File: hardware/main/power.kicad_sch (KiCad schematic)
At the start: 32 parts, among them Q1 SSM3J338R, Q2 BCP53, Q3 SSM3J338R, Q4 BC817, Q5 SSM3J338R, Q6 BC807, Q7 BC817, U5 AP2114H-3.3, U6 LM358

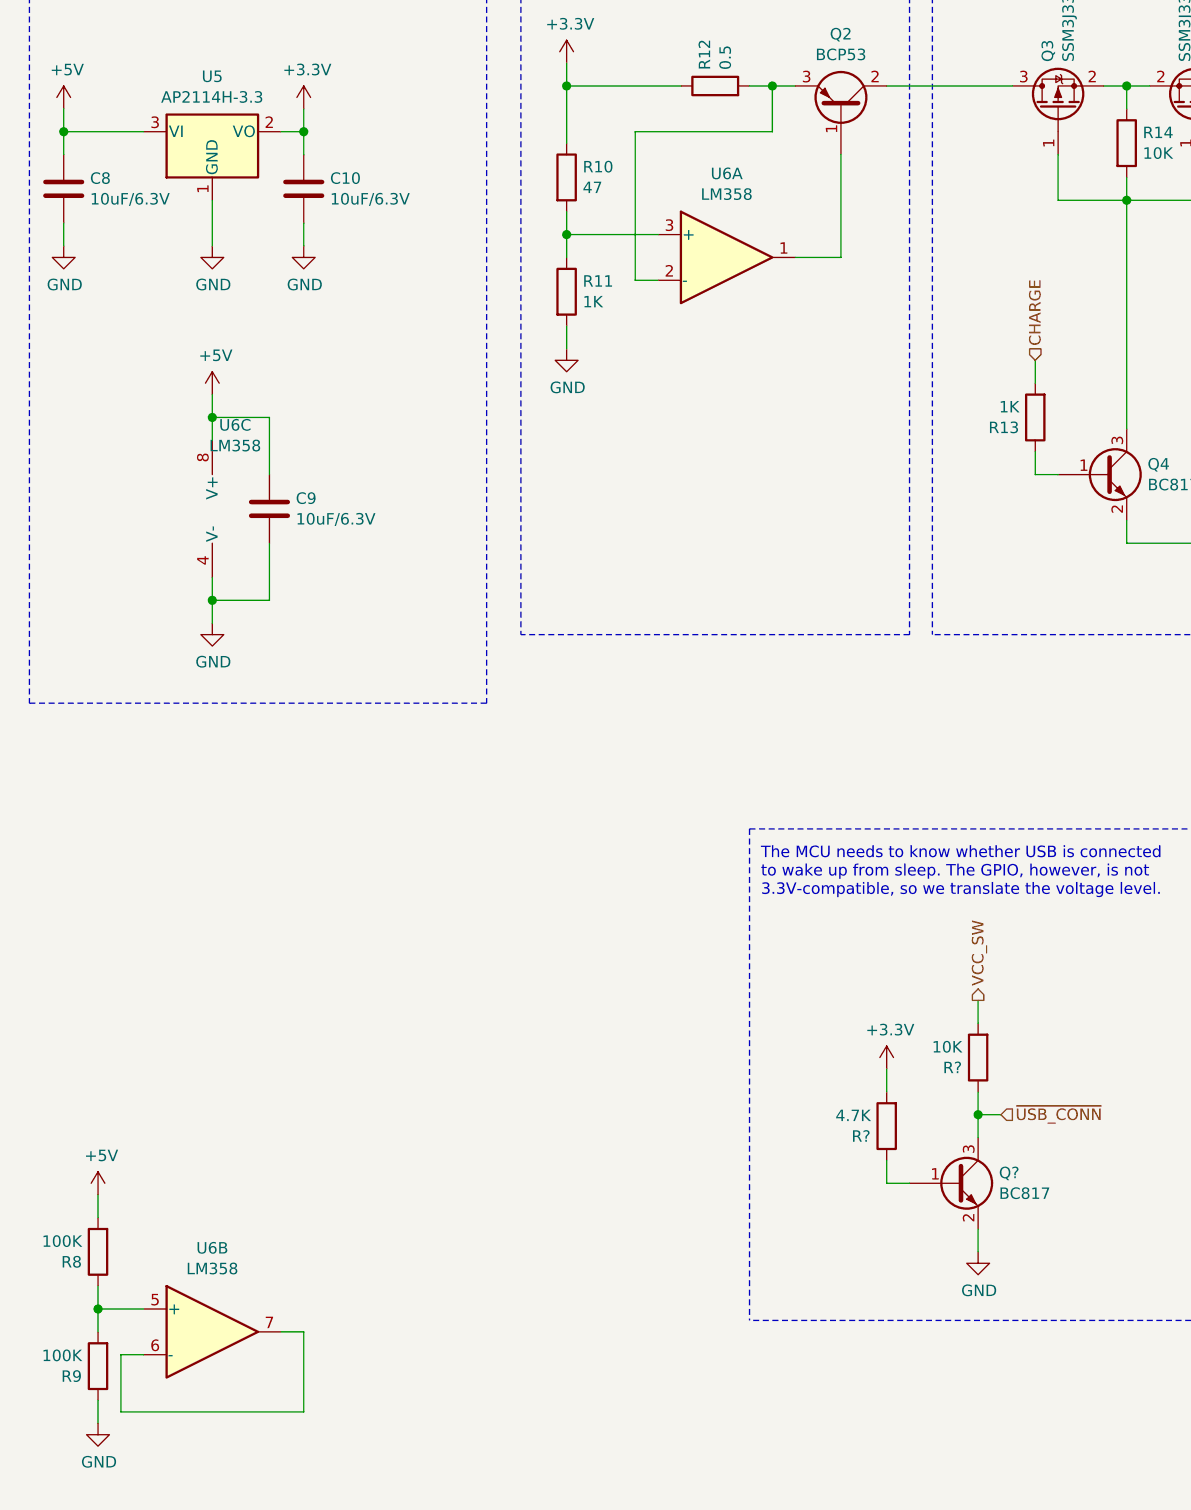
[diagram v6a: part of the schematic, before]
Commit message: Assign footprints
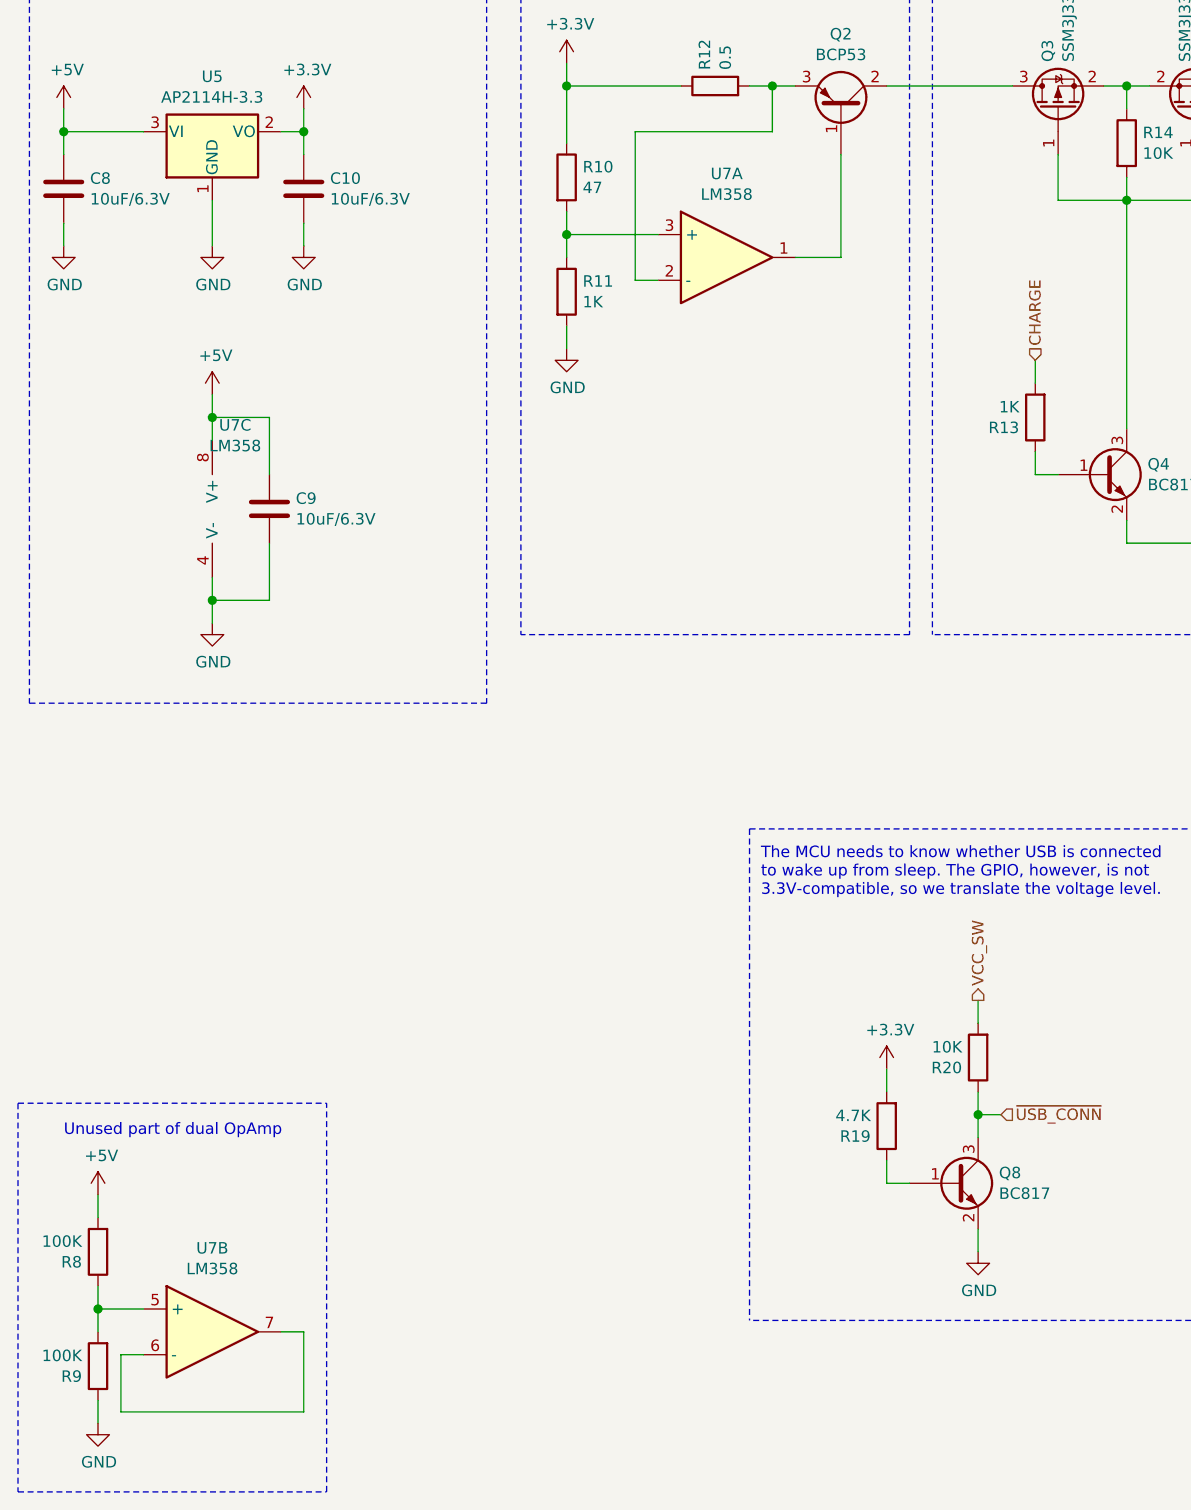
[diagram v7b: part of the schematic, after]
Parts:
- removed U6: LM358, symbol Amplifier_Operational:LM358
- added U7: LM358, symbol Device:Opamp_Dual
- gave numbers to parts that had none: 3
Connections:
- net +5V: now also U7.8 (V+)
- net GND: now also U7.4 (V-)
- net at R8.1, R9.2: now also U7.5 (+)
- net at R10.2, R11.1: now also U7.3 (+)
- net at Q2.1 (B): now also U7.1
- net at Q2.3 (E), R12.2: now also U7.2 (-)
- new net: U7.6 (-), U7.7
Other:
- note added: "Unused part of dual OpAmp"
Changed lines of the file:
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@@
     (stroke (width 0) (type solid) (color 0 0 0 0))
   )
+  (polyline (pts (xy 13.97 152.4) (xy 13.97 195.58))
+    (stroke (width 0) (type dash) (color 0 0 0 0))
+  )
+  (polyline (pts (xy 13.97 152.4) (xy 48.26 152.4))
+    (stroke (width 0) (type dash) (color 0 0 0 0))
+  )
+  (polyline (pts (xy 13.97 195.58) (xy 48.26 195.58))
+    (stroke (width 0) (type dash) (color 0 0 0 0))
+  )
   (polyline (pts (xy 15.24 17.78) (xy 15.24 107.95))
     (stroke (width 0) (type dash) (color 0 0 0 0))
   )
   (polyline (pts (xy 15.24 17.78) (xy 66.04 17.78))
+    (stroke (width 0) (type dash) (color 0 0 0 0))
+  )
+  (polyline (pts (xy 48.26 195.58) (xy 48.26 152.4))
     (stroke (width 0) (type dash) (color 0 0 0 0))
   )
@@
     (effects (font (size 1.27 1.27)) (justify left bottom))
   )
+  (text "Unused part of dual OpAmp" (at 19.05 156.21 0)
+    (effects (font (size 1.27 1.27)) (justify left bottom))
+  )
   (text "Constant current source - at 0.3A,\nthe sense resistor drops 0.15V."
     (at 71.12 24.13 0)
@@
   (symbol (lib_id "power:+3.3V") (at 110.49 148.59 0) (unit 1)
     (in_bom yes) (on_board yes)
-    (property "Reference" "#PWR?" (id 0) (at 110.49 152.4 0)
+    (property "Reference" "#PWR0140" (id 0) (at 110.49 152.4 0)
       (effects (font (size 1.27 1.27)) hide)
     )
@@
   (symbol (lib_id "power:GND") (at 120.65 168.91 0) (unit 1)
     (in_bom yes) (on_board yes)
-    (property "Reference" "#PWR?" (id 0) (at 120.65 175.26 0)
+    (property "Reference" "#PWR0141" (id 0) (at 120.65 175.26 0)
       (effects (font (size 1.27 1.27)) hide)
     )
@@
   (symbol (lib_id "Device:R") (at 110.49 154.94 180) (unit 1)
     (in_bom yes) (on_board yes)
-    (property "Reference" "R?" (id 0) (at 108.7119 156.0894 0)
+    (property "Reference" "R19" (id 0) (at 108.7119 156.0894 0)
       (effects (font (size 1.27 1.27)) (justify left))
     )
@@
   (symbol (lib_id "Device:R") (at 120.65 147.32 180) (unit 1)
     (in_bom yes) (on_board yes)
-    (property "Reference" "R?" (id 0) (at 118.8719 148.4694 0)
+    (property "Reference" "R20" (id 0) (at 118.8719 148.4694 0)
       (effects (font (size 1.27 1.27)) (justify left))
     )
@@
     )
   )
-  (symbol (lib_id "Amplifier_Operational:LM358") (at 38.1 86.36 0) (unit 3)
-    (in_bom yes) (on_board yes)
-    (property "Reference" "U6" (id 0) (at 38.1 77.0698 0))
+  (symbol (lib_id "Device:Opamp_Dual") (at 38.1 86.36 0) (unit 3)
+    (in_bom yes) (on_board yes)
+    (property "Reference" "U7" (id 0) (at 38.1 77.0698 0))
     (property "Value" "LM358" (id 1) (at 38.1 79.3685 0))
     (property "Footprint" "" (id 2) (at 38.1 86.36 0)
       (effects (font (size 1.27 1.27)) hide)
     )
-    (property "Datasheet" "http://www.ti.com/lit/ds/symlink/lm2904-n.pdf" (id 3) (at 38.1 86.36 0)
+    (property "Datasheet" "~" (id 3) (at 38.1 86.36 0)
       (effects (font (size 1.27 1.27)) hide)
     )
@@
   (symbol (lib_id "Transistor_BJT:BC817") (at 118.11 161.29 0) (unit 1)
     (in_bom yes) (on_board yes)
-    (property "Reference" "Q?" (id 0) (at 122.9615 160.1406 0)
+    (property "Reference" "Q8" (id 0) (at 122.9615 160.1406 0)
       (effects (font (size 1.27 1.27)) (justify left))
     )
@@
     )
   )
-  (symbol (lib_id "Amplifier_Operational:LM358") (at 35.56 177.8 0) (unit 2)
-    (in_bom yes) (on_board yes)
-    (property "Reference" "U6" (id 0) (at 35.56 168.5098 0))
-    (property "Value" "LM358" (id 1) (at 35.56 170.8085 0))
+  (symbol (lib_id "Device:Opamp_Dual") (at 35.56 177.8 0) (unit 2)
+    (in_bom yes) (on_board yes)
+    (property "Reference" "U7" (id 0) (at 35.56 168.5098 0))
+    (property "Value" "LM358" (id 1) (at 35.56 170.808 0))
     (property "Footprint" "" (id 2) (at 35.56 177.8 0)
       (effects (font (size 1.27 1.27)) hide)
     )
-    (property "Datasheet" "http://www.ti.com/lit/ds/symlink/lm2904-n.pdf" (id 3) (at 35.56 177.8 0)
-      (effects (font (size 1.27 1.27)) hide)
-    )
-  )
-  (symbol (lib_id "Amplifier_Operational:LM358") (at 92.71 58.42 0) (unit 1)
-    (in_bom yes) (on_board yes)
-    (property "Reference" "U6" (id 0) (at 92.71 49.1298 0))
+    (property "Datasheet" "~" (id 3) (at 35.56 177.8 0)
+      (effects (font (size 1.27 1.27)) hide)
+    )
+  )
+  (symbol (lib_id "Device:Opamp_Dual") (at 92.71 58.42 0) (unit 1)
+    (in_bom yes) (on_board yes)
+    (property "Reference" "U7" (id 0) (at 92.71 49.1298 0))
     (property "Value" "LM358" (id 1) (at 92.71 51.4285 0))
-    (property "Footprint" "" (id 2) (at 92.71 58.42 0)
-      (effects (font (size 1.27 1.27)) hide)
-    )
-    (property "Datasheet" "http://www.ti.com/lit/ds/symlink/lm2904-n.pdf" (id 3) (at 92.71 58.42 0)
-      (effects (font (size 1.27 1.27)) hide)
-    )
+    (property "Footprint" "Package_SO:TSSOP-8_4.4x3mm_P0.65mm" (id 2) (at 92.71 58.42 0)
+      (effects (font (size 1.27 1.27)) hide)
+    )
+    (property "Datasheet" "https://www.ti.com/lit/ds/symlink/lm358.pdf?HQS=dis-mous-null-mousermode-dsf-pf-null-wwe&ts=1611477242242" (id 3) (at 92.71 58.42 0)
+      (effects (font (size 1.27 1.27)) hide)
+    )
+    (property "Mouser" "595-LM358PW " (id 4) (at 92.71 58.42 0)
+      (effects (font (size 1.27 1.27)) hide)
+    )
+    (property "Part Name" "LM358PW" (id 5) (at 92.71 58.42 0)
+      (effects (font (size 1.27 1.27)) hide)
+    )
